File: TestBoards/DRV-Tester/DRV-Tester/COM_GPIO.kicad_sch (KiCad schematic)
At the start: 2 parts, among them J10 Conn_02x04_Odd_Even, J11 Conn_02x04_Odd_Even

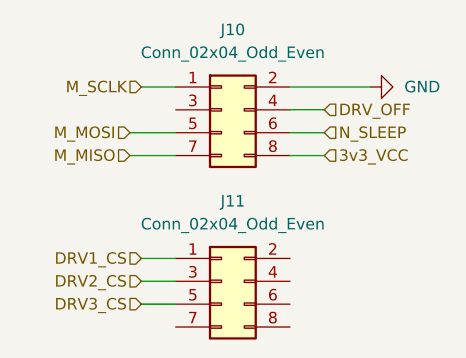
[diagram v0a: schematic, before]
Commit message: update tester board with layout
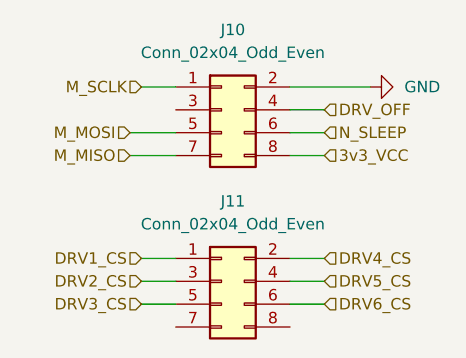
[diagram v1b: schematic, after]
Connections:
- net DRV4_CS: now reaches J11.2 (Pin_2)
- net DRV5_CS: now reaches J11.4 (Pin_4)
- net DRV6_CS: now reaches J11.6 (Pin_6)
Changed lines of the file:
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@@
+	(wire
+		(pts
+			(xy 140.97 99.06) (xy 137.16 99.06)
+		)
+		(stroke
+			(width 0)
+			(type default)
+		)
+	)
 	(wire
 		(pts
@@
 	(wire
 		(pts
+			(xy 140.97 101.6) (xy 137.16 101.6)
+		)
+		(stroke
+			(width 0)
+			(type default)
+		)
+	)
+	(wire
+		(pts
+			(xy 140.97 104.14) (xy 137.16 104.14)
+		)
+		(stroke
+			(width 0)
+			(type default)
+		)
+	)
+	(wire
+		(pts
 			(xy 137.16 87.63) (xy 140.97 87.63)
 		)
@@
 		)
 	)
+	(hierarchical_label "DRV5_CS"
+		(shape input)
+		(at 140.97 101.6 0)
+		(fields_autoplaced yes)
+		(effects
+			(font
+				(size 1.27 1.27)
+			)
+			(justify left)
+		)
+	)
+	(hierarchical_label "DRV6_CS"
+		(shape input)
+		(at 140.97 104.14 0)
+		(fields_autoplaced yes)
+		(effects
+			(font
+				(size 1.27 1.27)
+			)
+			(justify left)
+		)
+	)
 	(hierarchical_label "DRV2_CS"
 		(shape input)
@@
 		)
 	)
+	(hierarchical_label "DRV4_CS"
+		(shape input)
+		(at 140.97 99.06 0)
+		(fields_autoplaced yes)
+		(effects
+			(font
+				(size 1.27 1.27)
+			)
+			(justify left)
+		)
+	)

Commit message: add caps and LEDs to testboard
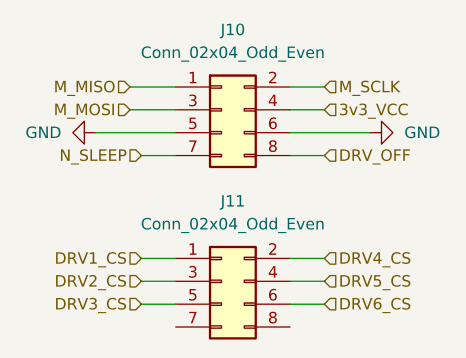
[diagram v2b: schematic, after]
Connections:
- net 3v3_VCC: now also J10.4 (Pin_4); no longer J10.8 (Pin_8)
- net DRV_OFF: now also J10.8 (Pin_8); no longer J10.4 (Pin_4)
- net GND: now also J10.5 (Pin_5), J10.6 (Pin_6); no longer J10.2 (Pin_2)
- net M_MISO: now also J10.1 (Pin_1); no longer J10.7 (Pin_7)
- net M_MOSI: now also J10.3 (Pin_3); no longer J10.5 (Pin_5)
- net M_SCLK: now also J10.2 (Pin_2); no longer J10.1 (Pin_1)
- net N_SLEEP: now also J10.7 (Pin_7); no longer J10.6 (Pin_6)
